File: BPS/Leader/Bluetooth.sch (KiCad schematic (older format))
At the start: 5 parts, among them U18 MCP112, U19 RN4871

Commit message: Renames bps master to bps leader:
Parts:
- U18: Mouser (none) -> https://www.mouser.com/ProductDetail/Microchip-Technology/M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
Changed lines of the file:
@@
 F 2 "Package_TO_SOT_SMD:SOT-23" H 3500 3900 50  0001 C CNN
 F 3 "http://ww1.microchip.com/downloads/en/DeviceDoc/20001889F.pdf" H 3500 3900 50  0001 C CNN
-F 4 "2.63" H 3500 3900 50  0001 C CNN "Threshold"
+F 4 "https://www.mouser.com/ProductDetail/Microchip-Technology/MCP112T-270E-LB?qs=X7k1PQjaM9f%252Bkma3gOGkcg%3D%3D" H 3500 3900 50  0001 C CNN "Mouser"
+F 5 "2.63" H 3500 3900 50  0001 C CNN "Threshold"
 	1    3500 3900
 	1    0    0    -1

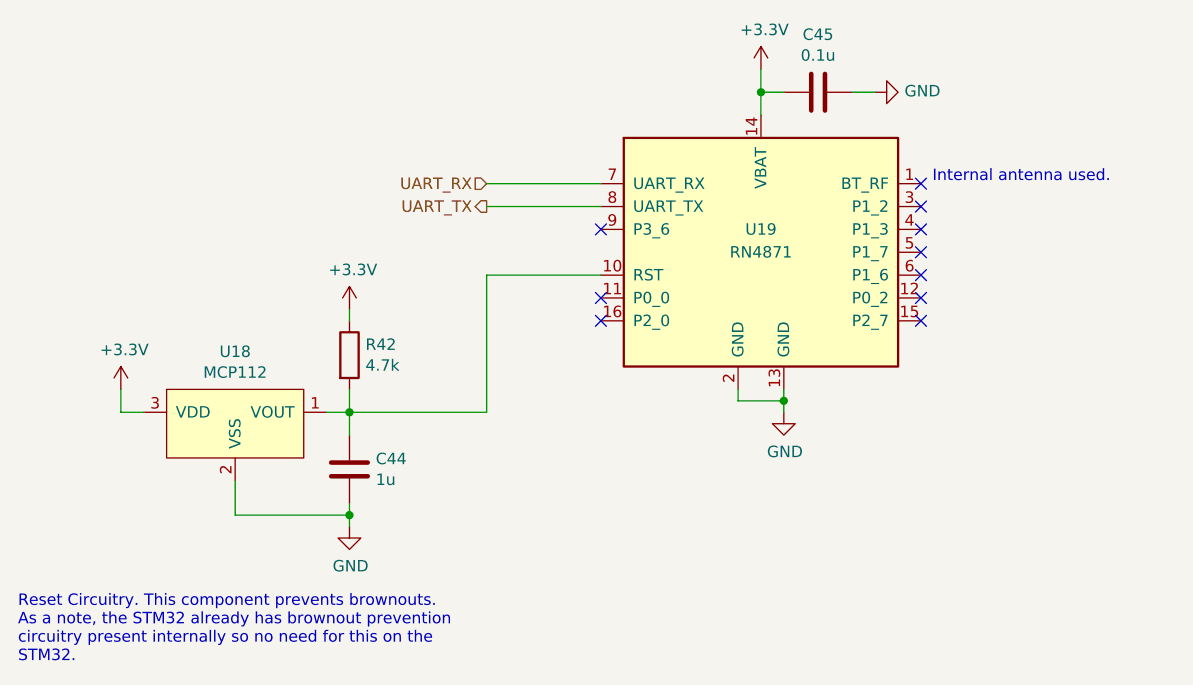
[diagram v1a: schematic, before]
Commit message: Places most components of leader board in their respective locations with nothing traced
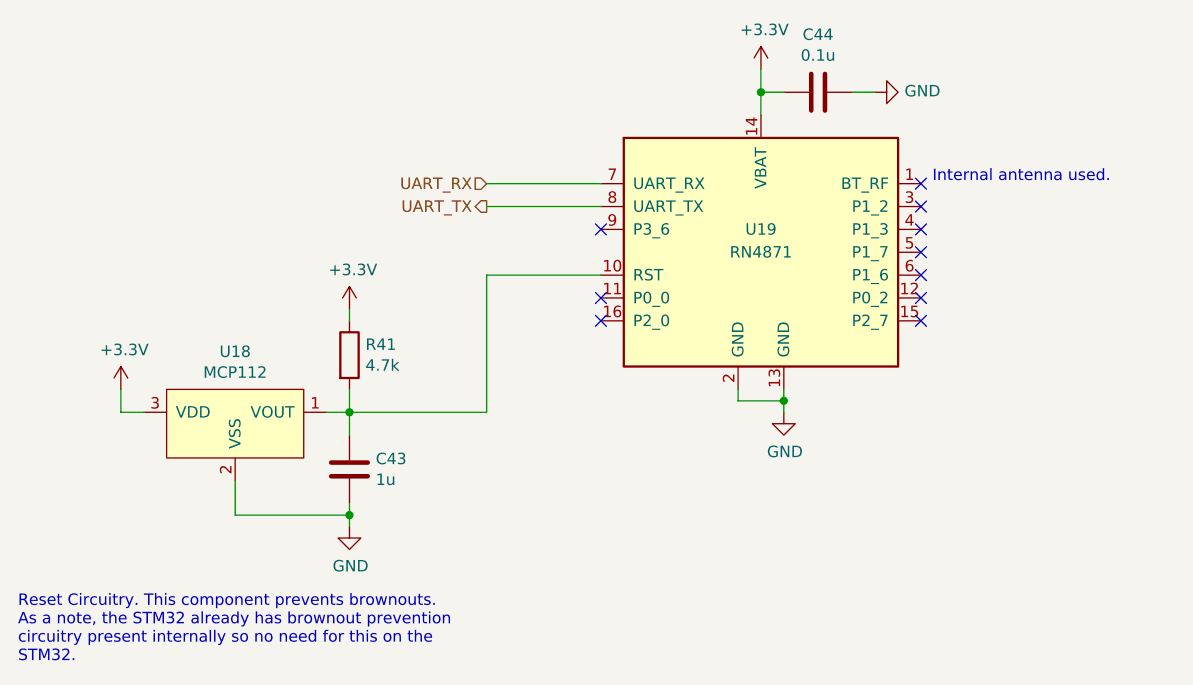
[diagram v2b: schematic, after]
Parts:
- renumbered C44 to C43, C45 to C44, R42 to R41
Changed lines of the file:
@@
 $EndComp
 $Comp
-L power:+3.3V #PWR0103
+L power:+3.3V #PWR0102
 U 1 1 5F24CC20
 P 5800 2500
-F 0 "#PWR0103" H 5800 2350 50  0001 C CNN
+F 0 "#PWR0102" H 5800 2350 50  0001 C CNN
 F 1 "+3.3V" H 5815 2673 50  0000 C CNN
 F 2 "" H 5800 2500 50  0001 C CNN
@@
 	5800 2500 5800 2600
 $Comp
-L Device:C C45
+L Device:C C44
 U 1 1 5F24D8BD
 P 6050 2600
-F 0 "C45" V 5798 2600 50  0000 C CNN
+F 0 "C44" V 5798 2600 50  0000 C CNN
 F 1 "0.1u" V 5889 2600 50  0000 C CNN
 F 2 "Capacitor_SMD:C_0805_2012Metric" H 6088 2450 50  0001 C CNN
@@
 	5800 2600 5800 2700
 $Comp
-L power:GND #PWR0105
+L power:GND #PWR0104
 U 1 1 5F24E813
 P 6300 2600
-F 0 "#PWR0105" H 6300 2350 50  0001 C CNN
+F 0 "#PWR0104" H 6300 2350 50  0001 C CNN
 F 1 "GND" V 6305 2472 50  0000 R CNN
 F 2 "" H 6300 2600 50  0001 C CNN
@@
 NoConn ~ 5100 3600
 $Comp
-L power:GND #PWR0104
+L power:GND #PWR0103
 U 1 1 5F2507B7
 P 5900 4000
-F 0 "#PWR0104" H 5900 3750 50  0001 C CNN
+F 0 "#PWR0103" H 5900 3750 50  0001 C CNN
 F 1 "GND" H 5905 3827 50  0000 C CNN
 F 2 "" H 5900 4000 50  0001 C CNN
@@
 $EndComp
 $Comp
-L power:+3.3V #PWR0100
+L power:+3.3V #PWR099
 U 1 1 5F2892CC
 P 3000 3900
-F 0 "#PWR0100" H 3000 3750 50  0001 C CNN
+F 0 "#PWR099" H 3000 3750 50  0001 C CNN
 F 1 "+3.3V" H 3015 4073 50  0000 C CNN
 F 2 "" H 3000 3900 50  0001 C CNN
@@
 	3000 4000 3100 4000
 $Comp
-L Device:R R42
+L Device:R R41
 U 1 1 5F28A0A0
 P 4000 3750
-F 0 "R42" H 4070 3796 50  0000 L CNN
+F 0 "R41" H 4070 3796 50  0000 L CNN
 F 1 "4.7k" H 4070 3705 50  0000 L CNN
 F 2 "Resistor_SMD:R_0805_2012Metric" V 3930 3750 50  0001 C CNN
@@
 $EndComp
 $Comp
-L Device:C C44
+L Device:C C43
 U 1 1 5F28A62D
 P 4000 4250
-F 0 "C44" H 4115 4296 50  0000 L CNN
+F 0 "C43" H 4115 4296 50  0000 L CNN
 F 1 "1u" H 4115 4205 50  0000 L CNN
 F 2 "Capacitor_SMD:C_0805_2012Metric" H 4038 4100 50  0001 C CNN
@@
 Connection ~ 4000 4000
 $Comp
-L power:GND #PWR0102
+L power:GND #PWR0101
 U 1 1 5F28AD68
 P 4000 4500
-F 0 "#PWR0102" H 4000 4250 50  0001 C CNN
+F 0 "#PWR0101" H 4000 4250 50  0001 C CNN
 F 1 "GND" H 4005 4327 50  0000 C CNN
 F 2 "" H 4000 4500 50  0001 C CNN
@@
 	4000 4450 4000 4400
 $Comp
-L power:+3.3V #PWR0101
+L power:+3.3V #PWR0100
 U 1 1 5F28BC6F
 P 4000 3550
-F 0 "#PWR0101" H 4000 3400 50  0001 C CNN
+F 0 "#PWR0100" H 4000 3400 50  0001 C CNN
 F 1 "+3.3V" H 4015 3723 50  0000 C CNN
 F 2 "" H 4000 3550 50  0001 C CNN

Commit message: Adds power planes
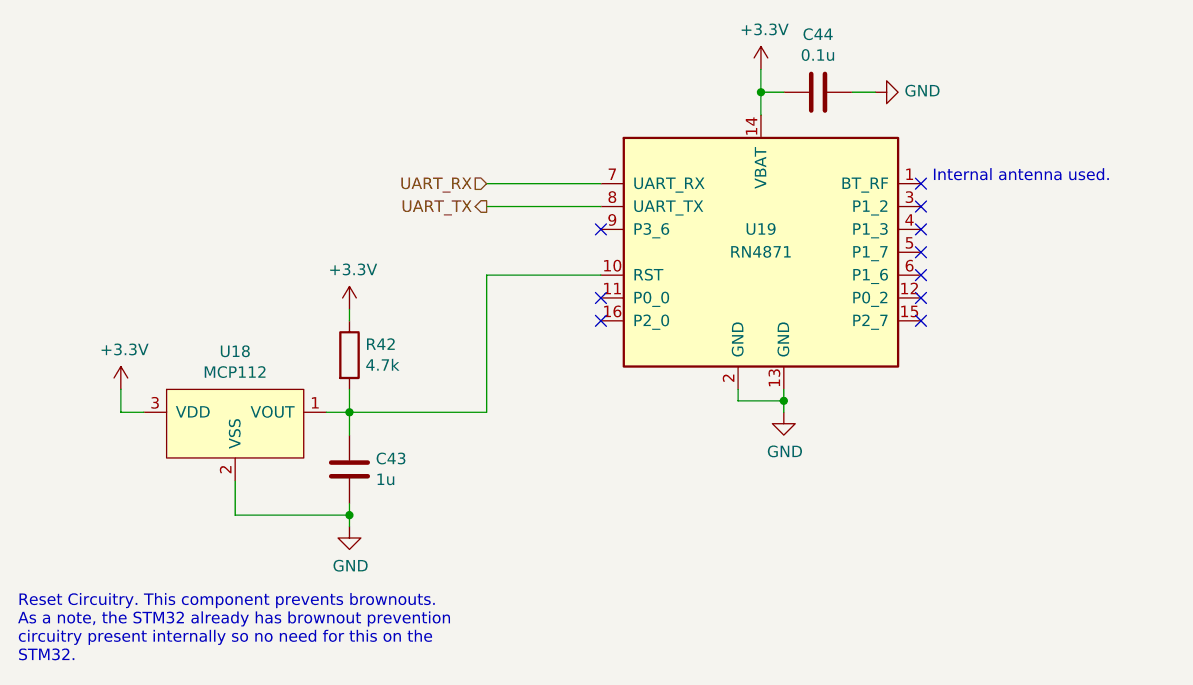
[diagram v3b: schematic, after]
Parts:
- renumbered R41 to R42
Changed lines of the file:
@@
 	3000 4000 3100 4000
 $Comp
-L Device:R R41
+L Device:R R42
 U 1 1 5F28A0A0
 P 4000 3750
-F 0 "R41" H 4070 3796 50  0000 L CNN
+F 0 "R42" H 4070 3796 50  0000 L CNN
 F 1 "4.7k" H 4070 3705 50  0000 L CNN
 F 2 "Resistor_SMD:R_0805_2012Metric" V 3930 3750 50  0001 C CNN

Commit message: Simplifies dc-dc converter schematics
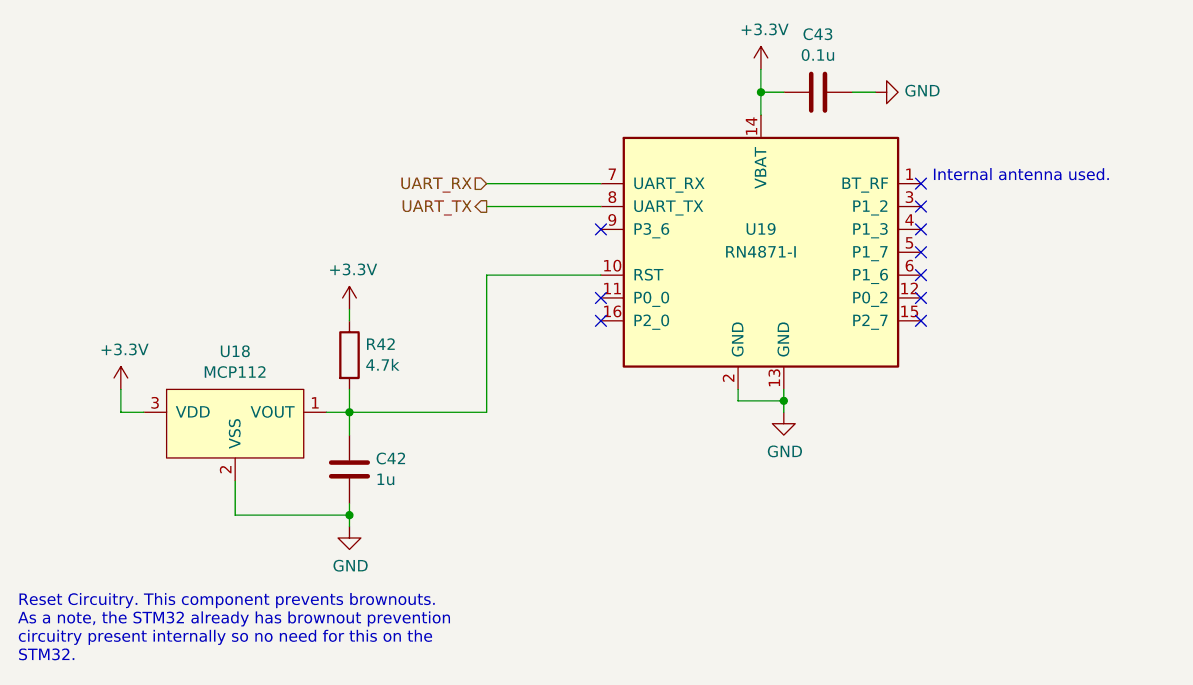
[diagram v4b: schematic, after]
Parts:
- U19: value RN4871 -> RN4871-I; Mouser (none) -> https://www.mouser.com/ProductDetail/Microchip-Technology/R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
- renumbered C43 to C42, C44 to C43
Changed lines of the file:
@@
 P 5800 3300
 F 0 "U19" H 5800 3400 50  0000 C CNN
-F 1 "RN4871" H 5800 3300 50  0000 C CNN
+F 1 "RN4871-I" H 5800 3300 50  0000 C CNN
 F 2 "RF_Module:Microchip_RN4871" H 5800 2600 50  0001 C CNN
 F 3 "http://ww1.microchip.com/downloads/en/DeviceDoc/50002489A.pdf" H 5300 3850 50  0001 C CNN
+F 4 "https://www.mouser.com/ProductDetail/Microchip-Technology/RN4871-I-RM130?qs=MLItCLRbWswoZsrzvVbGYw%3D%3D" H 5800 3300 50  0001 C CNN "Mouser"
 	1    5800 3300
 	1    0    0    -1
 $EndComp
 $Comp
-L power:+3.3V #PWR0102
+L power:+3.3V #PWR0101
 U 1 1 5F24CC20
 P 5800 2500
-F 0 "#PWR0102" H 5800 2350 50  0001 C CNN
+F 0 "#PWR0101" H 5800 2350 50  0001 C CNN
 F 1 "+3.3V" H 5815 2673 50  0000 C CNN
 F 2 "" H 5800 2500 50  0001 C CNN
@@
 	5800 2500 5800 2600
 $Comp
-L Device:C C44
+L Device:C C43
 U 1 1 5F24D8BD
 P 6050 2600
-F 0 "C44" V 5798 2600 50  0000 C CNN
+F 0 "C43" V 5798 2600 50  0000 C CNN
 F 1 "0.1u" V 5889 2600 50  0000 C CNN
 F 2 "Capacitor_SMD:C_0805_2012Metric" H 6088 2450 50  0001 C CNN
@@
 	5800 2600 5800 2700
 $Comp
-L power:GND #PWR0104
+L power:GND #PWR0103
 U 1 1 5F24E813
 P 6300 2600
-F 0 "#PWR0104" H 6300 2350 50  0001 C CNN
+F 0 "#PWR0103" H 6300 2350 50  0001 C CNN
 F 1 "GND" V 6305 2472 50  0000 R CNN
 F 2 "" H 6300 2600 50  0001 C CNN
@@
 NoConn ~ 5100 3600
 $Comp
-L power:GND #PWR0103
+L power:GND #PWR0102
 U 1 1 5F2507B7
 P 5900 4000
-F 0 "#PWR0103" H 5900 3750 50  0001 C CNN
+F 0 "#PWR0102" H 5900 3750 50  0001 C CNN
 F 1 "GND" H 5905 3827 50  0000 C CNN
 F 2 "" H 5900 4000 50  0001 C CNN
@@
 $EndComp
 $Comp
-L power:+3.3V #PWR099
+L power:+3.3V #PWR098
 U 1 1 5F2892CC
 P 3000 3900
-F 0 "#PWR099" H 3000 3750 50  0001 C CNN
+F 0 "#PWR098" H 3000 3750 50  0001 C CNN
 F 1 "+3.3V" H 3015 4073 50  0000 C CNN
 F 2 "" H 3000 3900 50  0001 C CNN
@@
 $EndComp
 $Comp
-L Device:C C43
+L Device:C C42
 U 1 1 5F28A62D
 P 4000 4250
-F 0 "C43" H 4115 4296 50  0000 L CNN
+F 0 "C42" H 4115 4296 50  0000 L CNN
 F 1 "1u" H 4115 4205 50  0000 L CNN
 F 2 "Capacitor_SMD:C_0805_2012Metric" H 4038 4100 50  0001 C CNN
@@
 Connection ~ 4000 4000
 $Comp
-L power:GND #PWR0101
+L power:GND #PWR0100
 U 1 1 5F28AD68
 P 4000 4500
-F 0 "#PWR0101" H 4000 4250 50  0001 C CNN
+F 0 "#PWR0100" H 4000 4250 50  0001 C CNN
 F 1 "GND" H 4005 4327 50  0000 C CNN
 F 2 "" H 4000 4500 50  0001 C CNN
@@
 	4000 4450 4000 4400
 $Comp
-L power:+3.3V #PWR0100
+L power:+3.3V #PWR099
 U 1 1 5F28BC6F
 P 4000 3550
-F 0 "#PWR0100" H 4000 3400 50  0001 C CNN
+F 0 "#PWR099" H 4000 3400 50  0001 C CNN
 F 1 "+3.3V" H 4015 3723 50  0000 C CNN
 F 2 "" H 4000 3550 50  0001 C CNN
